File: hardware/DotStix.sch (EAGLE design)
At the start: 9 parts, among them U1 ATMEGA328P-MU-QFN32

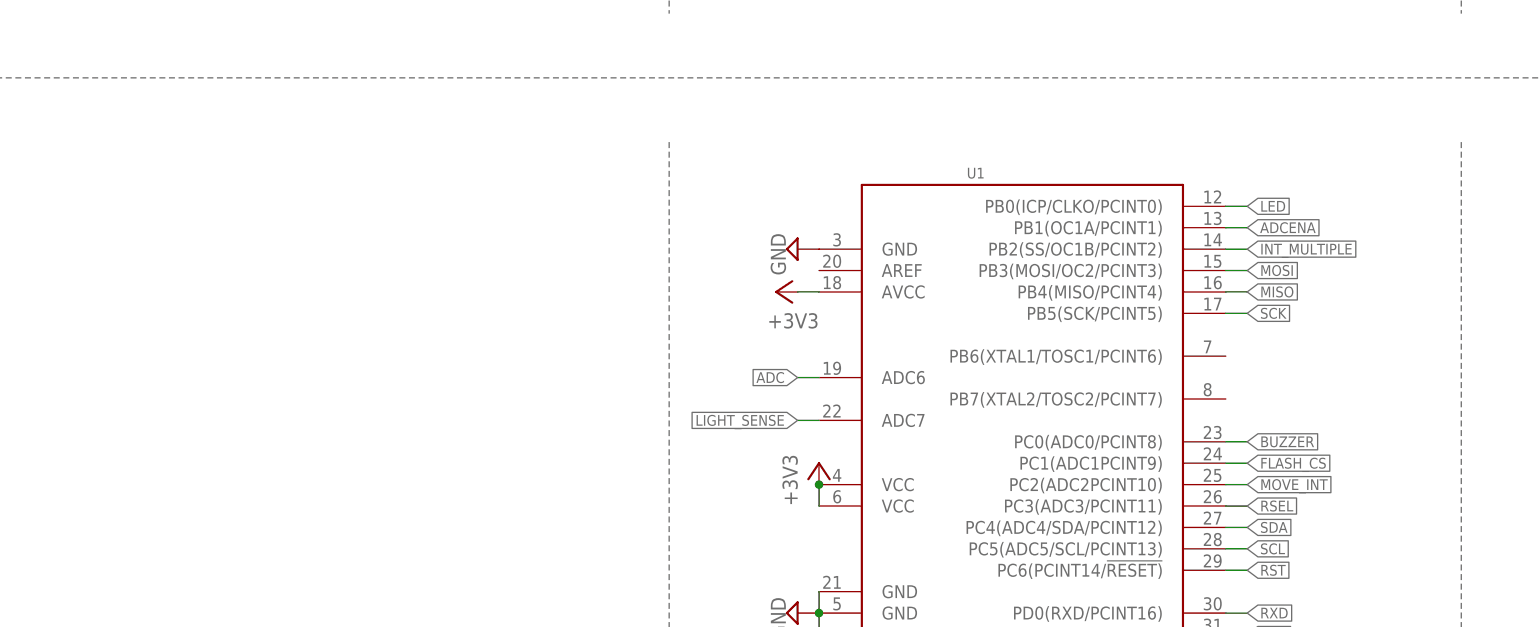
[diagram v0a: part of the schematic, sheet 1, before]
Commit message: Add reed switch
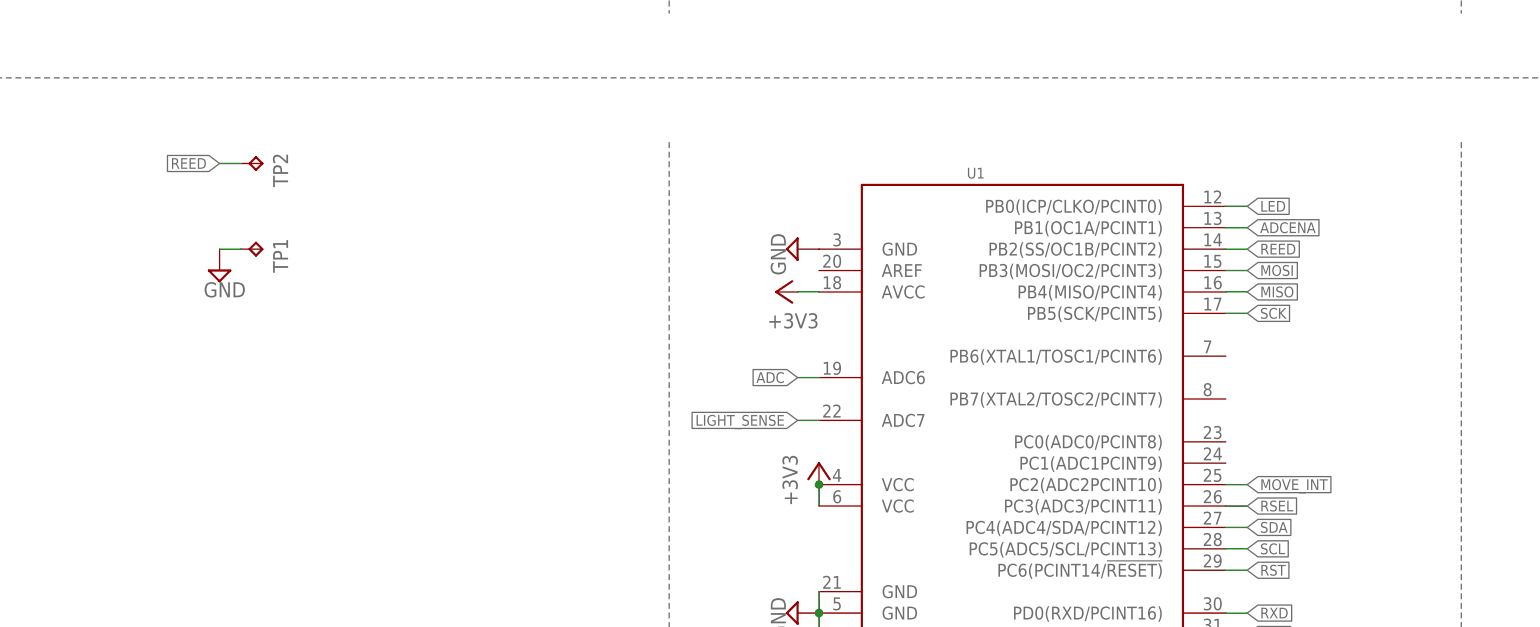
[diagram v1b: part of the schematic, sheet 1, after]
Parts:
- added TP1, TP2: TPTP20SQ, testpad:TPTP20SQ
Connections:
- removed net BUZZER: U1.PC0(ADC0/PCINT8)
- removed net FLASH_CS: U1.PC1(ADC1PCINT9)
- removed net INT_MULTIPLE: U1.PB2(SS/OC1B/PCINT2)
- new net REED: TP2.TP, U1.PB2(SS/OC1B/PCINT2)
- net GND: now also TP1.TP
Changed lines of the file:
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@@
 <part name="SUPPLY21" library="supply2" deviceset="GND" device=""/>
 <part name="+3V8" library="supply1" deviceset="+3V3" device=""/>
+<part name="TP1" library="testpad" deviceset="TP" device="TP20SQ"/>
+<part name="TP2" library="testpad" deviceset="TP" device="TP20SQ"/>
+<part name="SUPPLY5" library="supply2" deviceset="GND" device=""/>
 </parts>
 <sheets>
@@
 <instance part="SUPPLY21" gate="GND" x="-38.1" y="152.4"/>
 <instance part="+3V8" gate="G$1" x="-38.1" y="172.72"/>
+<instance part="TP1" gate="G$1" x="81.28" y="81.28" rot="R270"/>
+<instance part="TP2" gate="G$1" x="81.28" y="91.44" rot="R270"/>
+<instance part="SUPPLY5" gate="GND" x="76.2" y="78.74"/>
 </instances>
 <busses>
@@
 <wire x1="-38.1" y1="157.48" x2="-38.1" y2="154.94" width="0.1524" layer="91"/>
 </segment>
+<segment>
+<pinref part="TP1" gate="G$1" pin="TP"/>
+<pinref part="SUPPLY5" gate="GND" pin="GND"/>
+<wire x1="78.74" y1="81.28" x2="76.2" y2="81.28" width="0.1524" layer="91"/>
+</segment>
 </net>
 <net name="SDA" class="0">
@@
 </segment>
 </net>
-<net name="FLASH_CS" class="0">
-<segment>
-<pinref part="U1" gate="G$1" pin="PC1(ADC1PCINT9)"/>
-<wire x1="195.58" y1="55.88" x2="198.12" y2="55.88" width="0.1524" layer="91"/>
-<label x="198.12" y="55.88" size="1.27" layer="95" xref="yes"/>
-</segment>
-</net>
 <net name="ADC" class="0">
 <segment>
@@
 <wire x1="147.32" y1="66.04" x2="144.78" y2="66.04" width="0.1524" layer="91"/>
 <label x="144.78" y="66.04" size="1.27" layer="95" rot="R180" xref="yes"/>
-</segment>
-</net>
-<net name="BUZZER" class="0">
-<segment>
-<pinref part="U1" gate="G$1" pin="PC0(ADC0/PCINT8)"/>
-<wire x1="195.58" y1="58.42" x2="198.12" y2="58.42" width="0.1524" layer="91"/>
-<label x="198.12" y="58.42" size="1.27" layer="95" xref="yes"/>
-</segment>
-</net>
-<net name="INT_MULTIPLE" class="0">
-<segment>
-<pinref part="U1" gate="G$1" pin="PB2(SS/OC1B/PCINT2)"/>
-<wire x1="195.58" y1="81.28" x2="198.12" y2="81.28" width="0.1524" layer="91"/>
-<label x="198.12" y="81.28" size="1.27" layer="95" xref="yes"/>
 </segment>
 </net>
@@
 </segment>
 </net>
+<net name="REED" class="0">
+<segment>
+<pinref part="TP2" gate="G$1" pin="TP"/>
+<wire x1="78.74" y1="91.44" x2="76.2" y2="91.44" width="0.1524" layer="91"/>
+<label x="76.2" y="91.44" size="1.27" layer="95" rot="R180" xref="yes"/>
+</segment>
+<segment>
+<pinref part="U1" gate="G$1" pin="PB2(SS/OC1B/PCINT2)"/>
+<wire x1="195.58" y1="81.28" x2="198.12" y2="81.28" width="0.1524" layer="91"/>
+<label x="198.12" y="81.28" size="1.27" layer="95" xref="yes"/>
+</segment>
+</net>

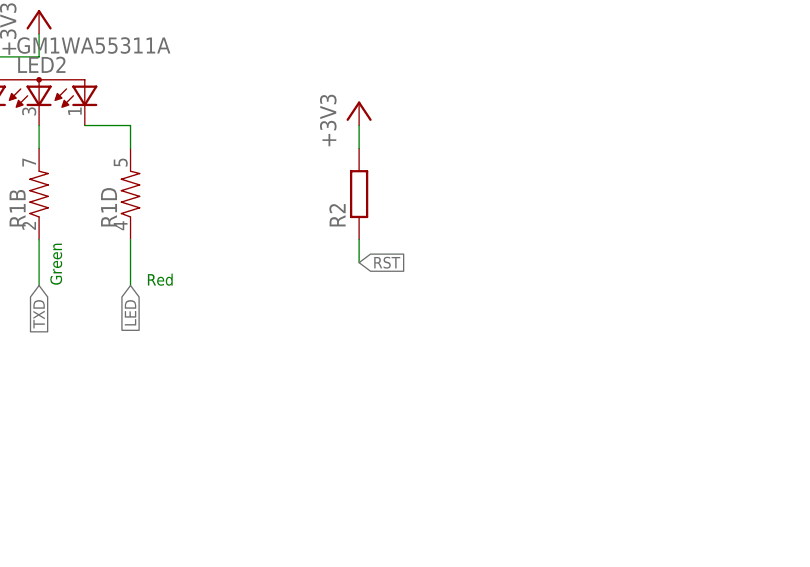
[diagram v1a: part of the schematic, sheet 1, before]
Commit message: Add RST switch
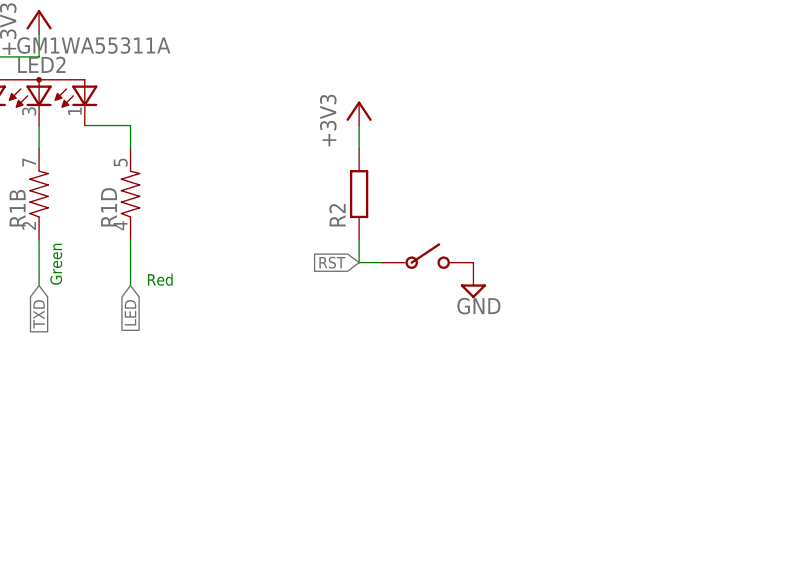
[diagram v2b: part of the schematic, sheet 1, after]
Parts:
- added U$3: PUSHBUTTON_4X2.5, pusbbutton_4x2_5:PUSHBUTTON_4X2.5
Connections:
- net GND: now also U$3.P$2
- net RST: now also U$3.P$1
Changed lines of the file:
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@@
 <part name="TP2" library="testpad" deviceset="TP" device="TP20SQ"/>
 <part name="SUPPLY5" library="supply2" deviceset="GND" device=""/>
+<part name="U$3" library="pusbbutton_4x2_5" deviceset="PUSHBUTTON_4X2.5" device=""/>
+<part name="SUPPLY7" library="supply2" deviceset="GND" device=""/>
 </parts>
 <sheets>
@@
 <instance part="TP2" gate="G$1" x="81.28" y="91.44" rot="R270"/>
 <instance part="SUPPLY5" gate="GND" x="76.2" y="78.74"/>
+<instance part="U$3" gate="G$1" x="78.74" y="154.94"/>
+<instance part="SUPPLY7" gate="GND" x="83.82" y="152.4"/>
 </instances>
 <busses>
@@
 <wire x1="78.74" y1="81.28" x2="76.2" y2="81.28" width="0.1524" layer="91"/>
 </segment>
+<segment>
+<pinref part="U$3" gate="G$1" pin="P$2"/>
+<pinref part="SUPPLY7" gate="GND" pin="GND"/>
+</segment>
 </net>
 <net name="SDA" class="0">
@@
 <pinref part="R2" gate="G$1" pin="1"/>
 <wire x1="71.12" y1="157.48" x2="71.12" y2="154.94" width="0.1524" layer="91"/>
-<label x="71.12" y="154.94" size="1.27" layer="95" xref="yes"/>
+<label x="71.12" y="154.94" size="1.27" layer="95" rot="R180" xref="yes"/>
 </segment>
 <segment>
@@
 <label x="11.43" y="77.47" size="1.27" layer="95" rot="R180" xref="yes"/>
 </segment>
+<segment>
+<pinref part="U$3" gate="G$1" pin="P$1"/>
+<wire x1="73.66" y1="154.94" x2="71.12" y2="154.94" width="0.1524" layer="91"/>
+</segment>
 </net>

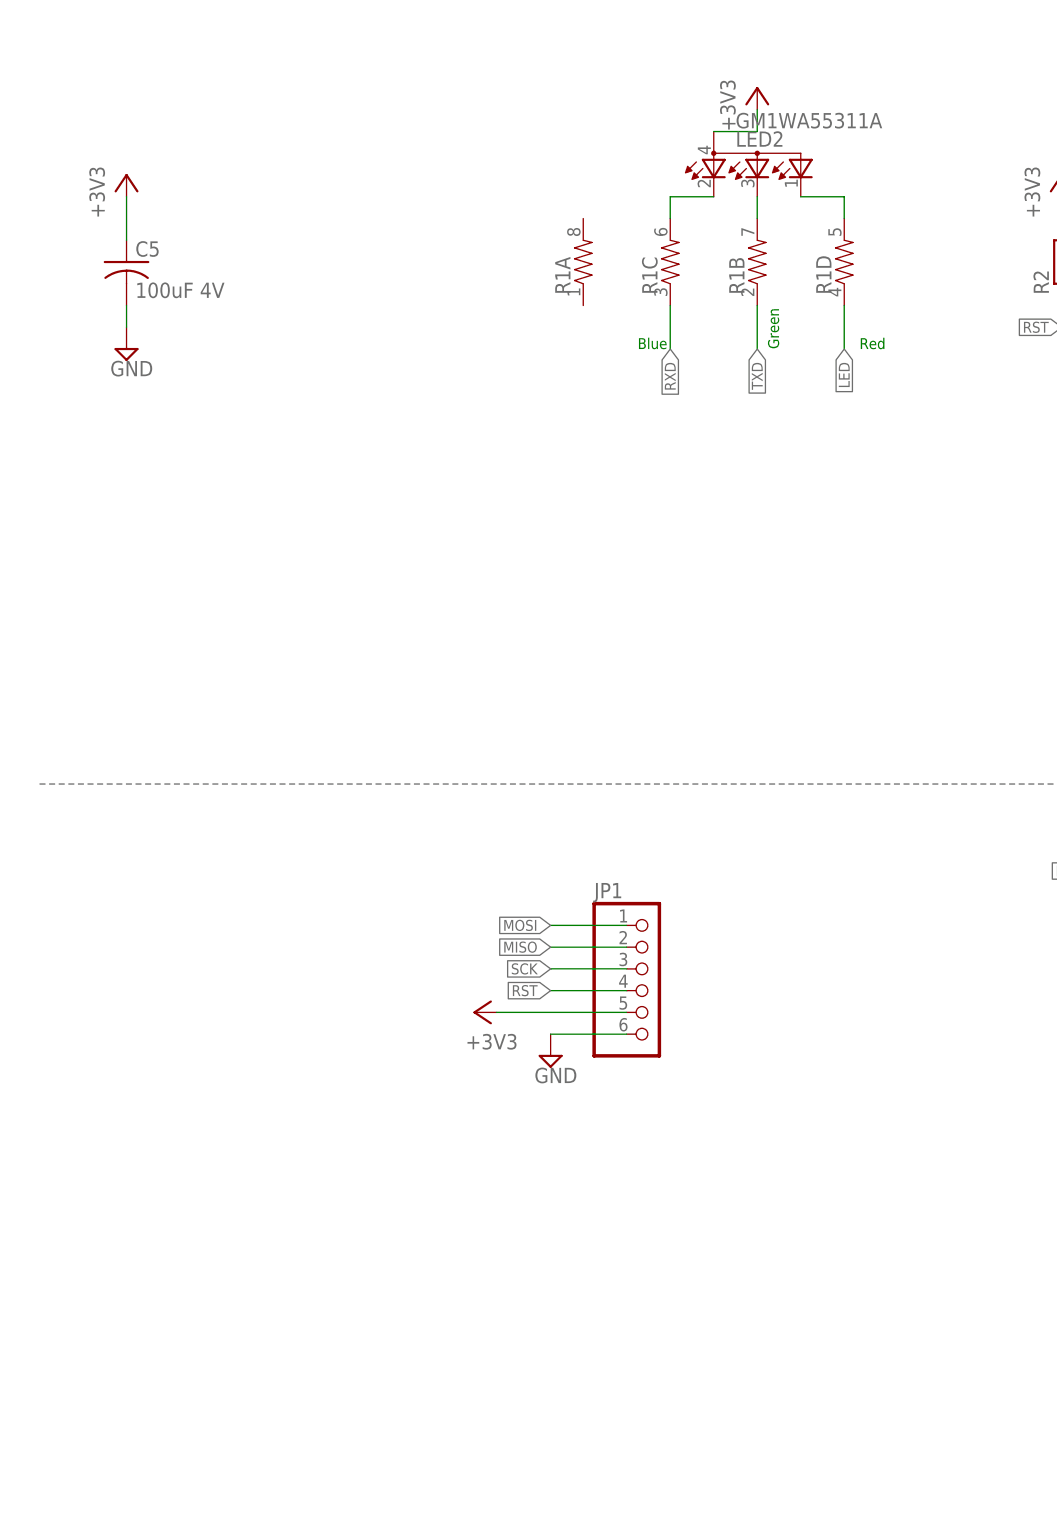
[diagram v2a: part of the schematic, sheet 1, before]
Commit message: Major rework, add solar cell
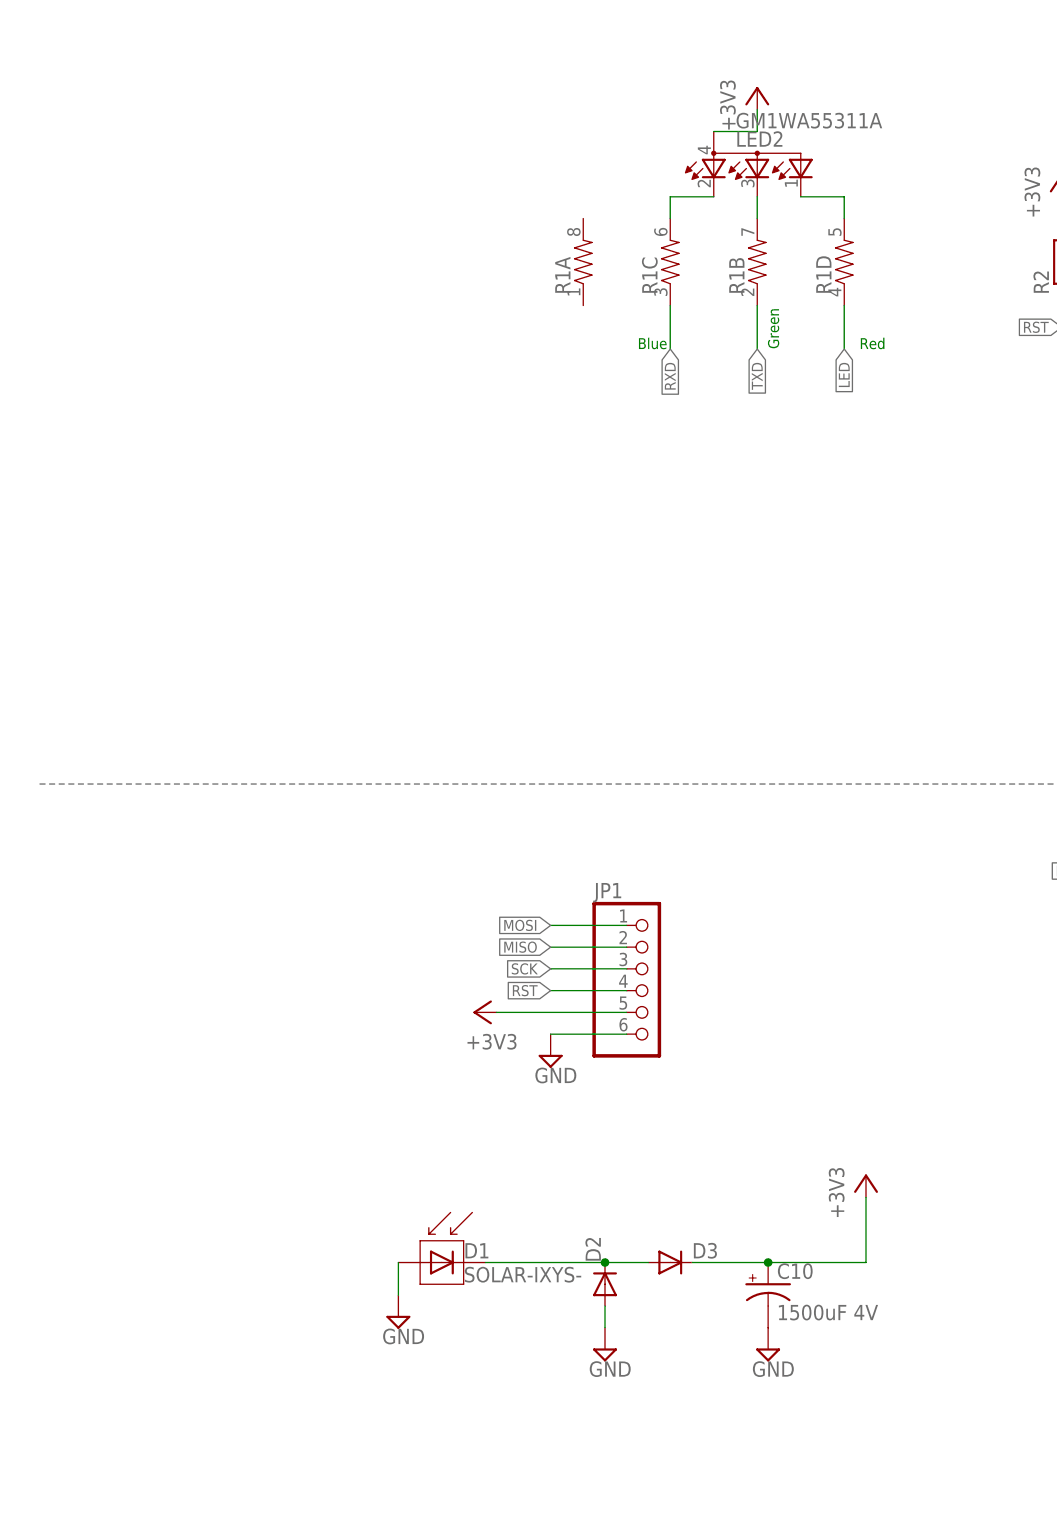
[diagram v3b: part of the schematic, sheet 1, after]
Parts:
- removed C5: 100uF 4V, adafruit:C-USC3216
- added C10: 1500uF 4V, adafruit:CPOL-USCT7343
- added D1: SOLAR-IXYS-, SparkFun:SOLAR-IXYS-
- added D2, D3: (no value), diode:DIODE-SOD523
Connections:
- new net SOLAR_RAW: D1.C, D2.C, D3.A
- net +3V3: now also C10.+, D3.C; no longer C5.1
- net GND: now also C10.-, D1.A, D2.A; no longer C5.2
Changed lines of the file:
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@@
 <setting verticaltext="up"/>
 </settings>
-<grid distance="0.1" unitdist="inch" unit="inch" style="lines" multiple="1" display="no" altdistance="0.01" altunitdist="inch" altunit="inch"/>
+<grid distance="0.05" unitdist="inch" unit="inch" style="lines" multiple="1" display="no" altdistance="0.01" altunitdist="inch" altunit="inch"/>
 <layers>
 <layer number="1" name="Top" color="4" fill="1" visible="no" active="no"/>
@@
 <part name="+3V7" library="supply1" deviceset="+3V3" device=""/>
 <part name="SUPPLY2" library="supply2" deviceset="GND" device=""/>
-<part name="C5" library="adafruit" deviceset="C-US" device="C3216" value="100uF 4V"/>
-<part name="SUPPLY21" library="supply2" deviceset="GND" device=""/>
-<part name="+3V8" library="supply1" deviceset="+3V3" device=""/>
 <part name="TP1" library="testpad" deviceset="TP" device="TP20SQ"/>
 <part name="TP2" library="testpad" deviceset="TP" device="TP20SQ"/>
@@
 <part name="U$3" library="pusbbutton_4x2_5" deviceset="PUSHBUTTON_4X2.5" device=""/>
 <part name="SUPPLY7" library="supply2" deviceset="GND" device=""/>
+<part name="D1" library="SparkFun" deviceset="SOLAR-IXYS" device="-"/>
+<part name="D2" library="diode" deviceset="DIODE-" device="SOD523"/>
+<part name="SUPPLY8" library="supply2" deviceset="GND" device=""/>
+<part name="C10" library="adafruit" deviceset="CPOL-US" device="CT7343" value="1500uF 4V"/>
+<part name="D3" library="diode" deviceset="DIODE-" device="SOD523"/>
+<part name="SUPPLY9" library="supply2" deviceset="GND" device=""/>
+<part name="+3V9" library="supply1" deviceset="+3V3" device=""/>
+<part name="SUPPLY10" library="supply2" deviceset="GND" device=""/>
 </parts>
 <sheets>
@@
 <instance part="+3V7" gate="G$1" x="2.54" y="74.93" rot="R90"/>
 <instance part="SUPPLY2" gate="GND" x="11.43" y="69.85"/>
-<instance part="C5" gate="G$1" x="-38.1" y="162.56"/>
-<instance part="SUPPLY21" gate="GND" x="-38.1" y="152.4"/>
-<instance part="+3V8" gate="G$1" x="-38.1" y="172.72"/>
 <instance part="TP1" gate="G$1" x="81.28" y="81.28" rot="R270"/>
 <instance part="TP2" gate="G$1" x="81.28" y="91.44" rot="R270"/>
@@
 <instance part="U$3" gate="G$1" x="78.74" y="154.94"/>
 <instance part="SUPPLY7" gate="GND" x="83.82" y="152.4"/>
+<instance part="D1" gate="G$1" x="-1.27" y="45.72"/>
+<instance part="D2" gate="G$1" x="17.78" y="43.18" rot="R90"/>
+<instance part="SUPPLY8" gate="GND" x="17.78" y="35.56"/>
+<instance part="C10" gate="G$1" x="36.83" y="43.18"/>
+<instance part="D3" gate="G$1" x="25.4" y="45.72"/>
+<instance part="SUPPLY9" gate="GND" x="36.83" y="35.56"/>
+<instance part="+3V9" gate="G$1" x="48.26" y="55.88"/>
+<instance part="SUPPLY10" gate="GND" x="-6.35" y="39.37"/>
 </instances>
 <busses>
@@
 </segment>
 <segment>
-<pinref part="C5" gate="G$1" pin="2"/>
-<pinref part="SUPPLY21" gate="GND" pin="GND"/>
-<wire x1="-38.1" y1="157.48" x2="-38.1" y2="154.94" width="0.1524" layer="91"/>
-</segment>
-<segment>
 <pinref part="TP1" gate="G$1" pin="TP"/>
 <pinref part="SUPPLY5" gate="GND" pin="GND"/>
@@
 <pinref part="U$3" gate="G$1" pin="P$2"/>
 <pinref part="SUPPLY7" gate="GND" pin="GND"/>
+</segment>
+<segment>
+<pinref part="D2" gate="G$1" pin="A"/>
+<pinref part="SUPPLY8" gate="GND" pin="GND"/>
+<wire x1="17.78" y1="38.1" x2="17.78" y2="40.64" width="0.1524" layer="91"/>
+</segment>
+<segment>
+<pinref part="C10" gate="G$1" pin="-"/>
+<pinref part="SUPPLY9" gate="GND" pin="GND"/>
+</segment>
+<segment>
+<pinref part="D1" gate="G$1" pin="A"/>
+<pinref part="SUPPLY10" gate="GND" pin="GND"/>
+<wire x1="-6.35" y1="45.72" x2="-6.35" y2="41.91" width="0.1524" layer="91"/>
 </segment>
 </net>
@@
 </segment>
 <segment>
-<pinref part="+3V8" gate="G$1" pin="+3V3"/>
-<pinref part="C5" gate="G$1" pin="1"/>
-<wire x1="-38.1" y1="170.18" x2="-38.1" y2="165.1" width="0.1524" layer="91"/>
+<pinref part="D3" gate="G$1" pin="C"/>
+<wire x1="27.94" y1="45.72" x2="36.83" y2="45.72" width="0.1524" layer="91"/>
+<pinref part="C10" gate="G$1" pin="+"/>
+<wire x1="36.83" y1="45.72" x2="48.26" y2="45.72" width="0.1524" layer="91"/>
+<junction x="36.83" y="45.72"/>
+<pinref part="+3V9" gate="G$1" pin="+3V3"/>
+<wire x1="48.26" y1="53.34" x2="48.26" y2="45.72" width="0.1524" layer="91"/>
 </segment>
 </net>
@@
 </segment>
 </net>
+<net name="SOLAR_RAW" class="0">
+<segment>
+<pinref part="D2" gate="G$1" pin="C"/>
+<wire x1="17.78" y1="45.72" x2="22.86" y2="45.72" width="0.1524" layer="91"/>
+<pinref part="D3" gate="G$1" pin="A"/>
+<pinref part="D1" gate="G$1" pin="C"/>
+<wire x1="3.81" y1="45.72" x2="17.78" y2="45.72" width="0.1524" layer="91"/>
+<junction x="17.78" y="45.72"/>
+</segment>
+</net>
